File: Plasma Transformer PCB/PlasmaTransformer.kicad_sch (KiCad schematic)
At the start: 86 parts, among them J1 Barrel_Jack_MountingPin, J10 Conn_01x01_Socket, J11 Screw_Terminal_01x01, J12 Screw_Terminal_01x01, J13 Conn_01x01_Socket, J14 Conn_01x01_Socket, J15 Conn_01x01_Socket, J16 Conn_01x01_Socket, J17 Conn_01x01_Socket, J18 Conn_01x01_Socket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

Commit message: WIP rev
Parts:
- removed H2: Hole_Heatsink_Screw, MountingHole:MountingHole_8.4mm_M8, symbol Mechanical:MountingHole
- removed HS1: Heatsink, Library:Heatsink_75x37.5mm_Fischer_SK-594-37.5-AL, symbol Mechanical:Heatsink
- added R11: 0.05, Resistor_SMD:R_2512_6332Metric, symbol Device:R
- added U2: LM358, symbol Amplifier_Operational:LM358
- C10, C7, C8, C9: footprint Capacitor_SMD:C_1812_4532Metric -> Capacitor_SMD:C_1206_3216Metric; MPN CC1812JKNPOCBN221 -> VJ1206A221JBGTW1HV; Manufacturer Yageo -> Vishay
- C11, C12, C21: footprint Capacitor_SMD:C_1812_4532Metric -> Capacitor_SMD:C_0805_2012Metric; MPN VJ1812A102JXFTW1HV -> CL21C102JCFNNNE; Manufacturer Vishay -> Samsung; Voltage 2000V -> 100V
- C3: value 2.7nF -> 3.3nF; footprint Capacitor_SMD:C_1812_4532Metric -> Capacitor_SMD:C_1206_3216Metric; Dielectric X7R -> NP0; MPN 1812GC272KAT1A -> C3216C0G2E332K085AA; Manufacturer Kyocera -> TDK; Voltage 2000V -> 250V
- C4: value 1.8nF -> 3.3nF; footprint Capacitor_SMD:C_1812_4532Metric -> Capacitor_SMD:C_1206_3216Metric; MPN C1812C182JCGACTU -> C3216C0G2E332K085AA; Manufacturer Kemet -> TDK; Voltage 500V -> 250V
- C5, C6: footprint Capacitor_SMD:C_1812_4532Metric -> Capacitor_SMD:C_1206_3216Metric; MPN C1812C182JCGACTU -> CC1206JKNPOZBN182; Manufacturer Kemet -> Yageo; Voltage 500V -> 630V
- Q1: footprint Package_TO_SOT_THT:TO-247-3_Horizontal_TabDown -> Package_TO_SOT_SMD:Infineon_PG-HSOF-8-2_ThermalVias; symbol Transistor_FET_Other:Q_NMOS_Depletion_GDS -> ALibrary:IMT40R025M2HXTMA1; MPN IRFP260NPBF -> IMT40R025M2HXTMA1
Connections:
- net DRAIN: now also Q1.4 (S); no longer Q1.2 (D)
- net GND: now also Q1.2 (SS), Q1.4 (S), R11.2; no longer J1.2
- new net GND-IN: J1.2, R11.1
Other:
- note added: "PLASMA TRANSFORMER REV 6"
- note removed: "Hole for TO-247 screw to heatsink"
- note removed: "PLASMA TRANSFORMER REV 5"
- moved on the sheet: D2, J1, SW1

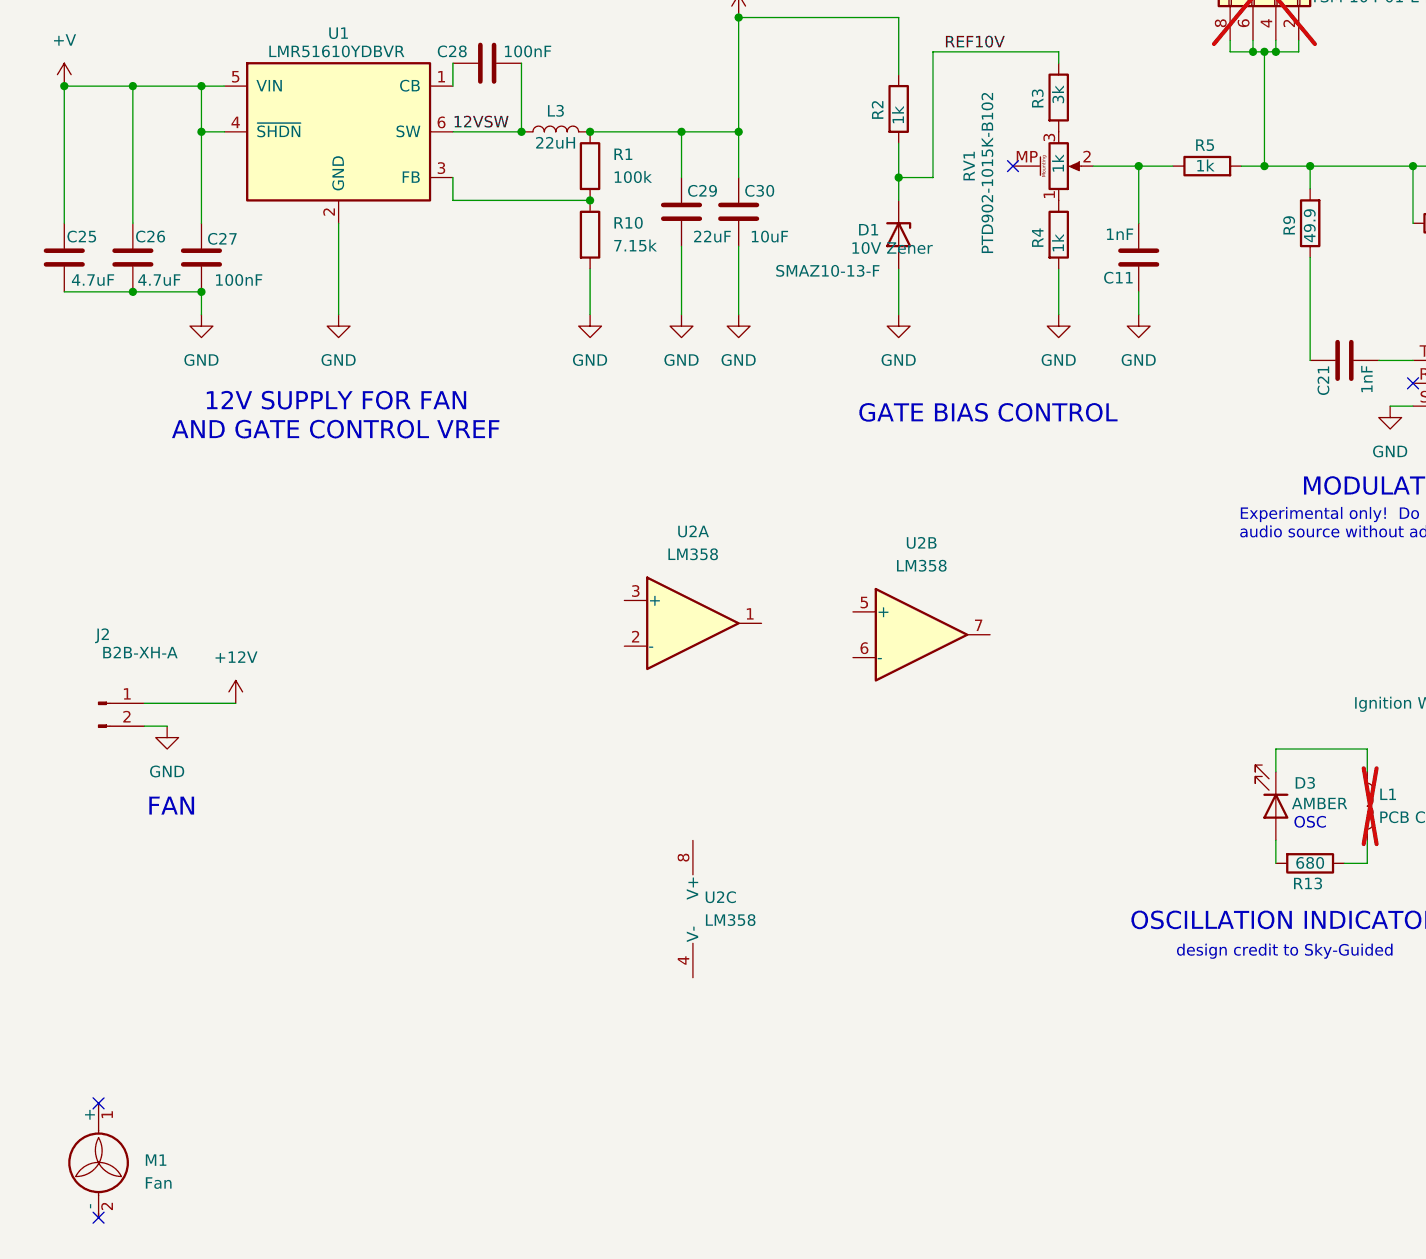
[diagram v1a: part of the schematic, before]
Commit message: mounting holes and silkscreens
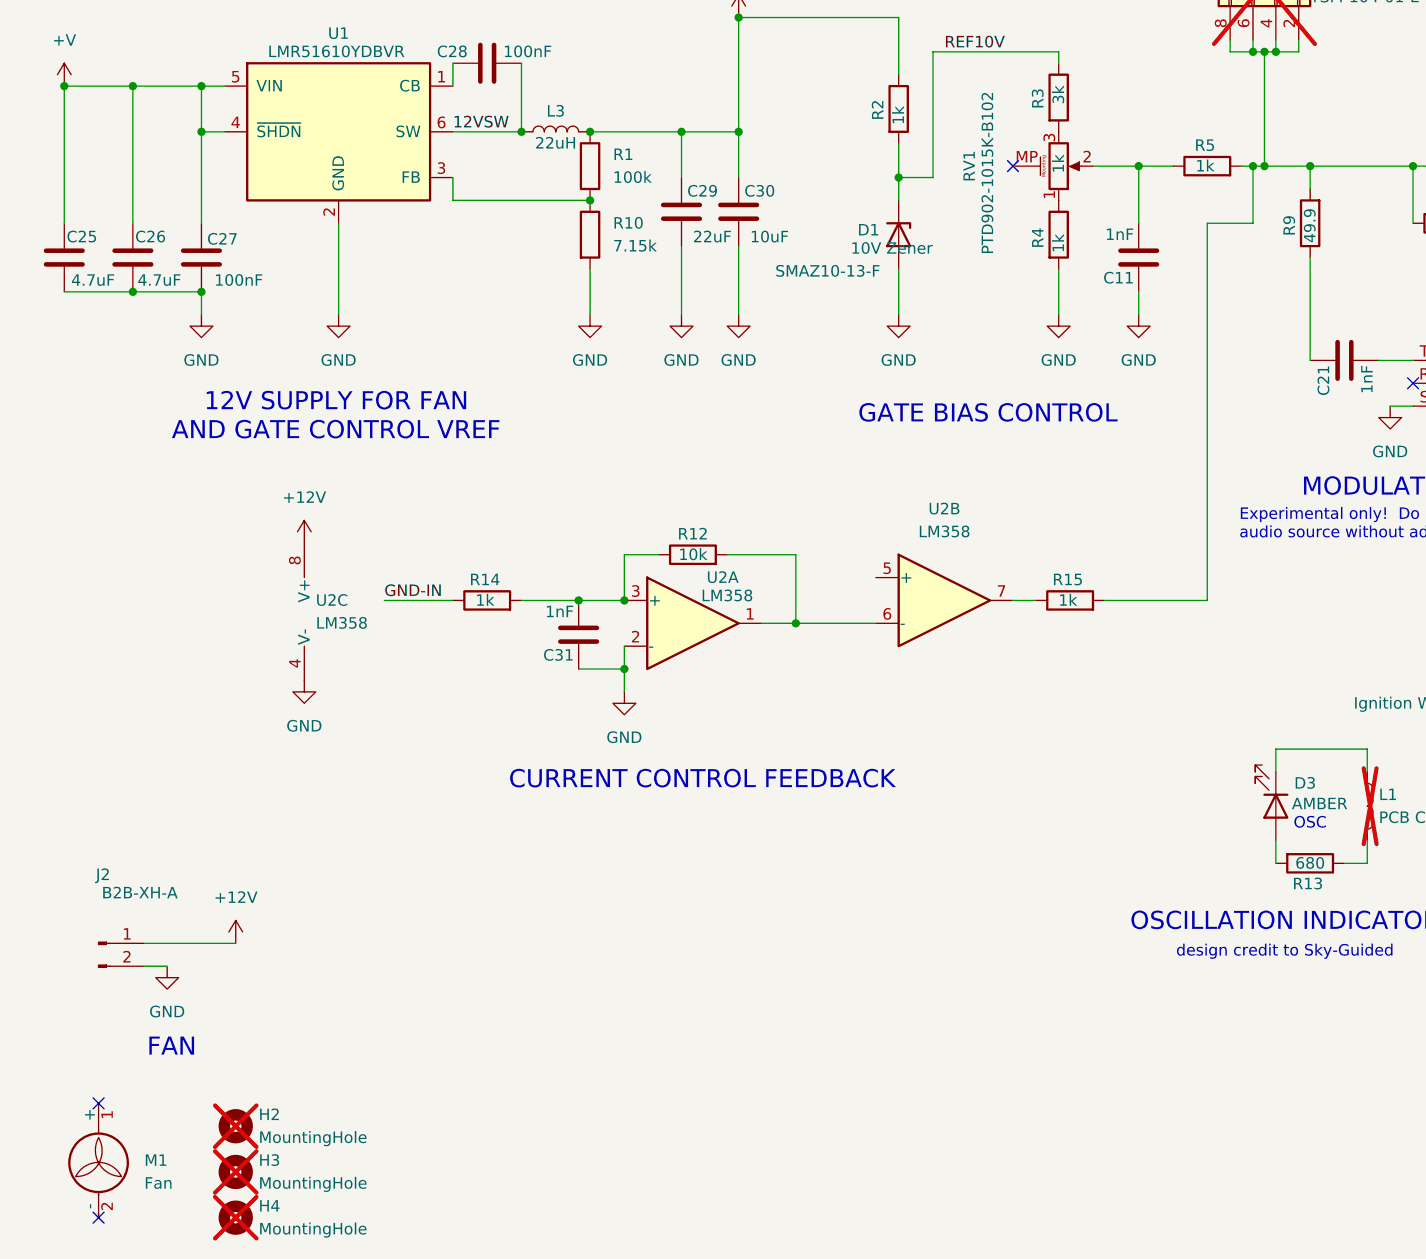
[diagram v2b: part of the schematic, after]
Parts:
- added C31: 1nF, Capacitor_SMD:C_0805_2012Metric, symbol Device:C
- added H2, H3, H4: MountingHole, MountingHole:MountingHole_3.2mm_M3, symbol Mechanical:MountingHole
- added R12: 10k, symbol Device:R
- added R14, R15: 1k, Resistor_SMD:R_0805_2012Metric, symbol Device:R
- Q1: footprint Package_TO_SOT_SMD:Infineon_PG-HSOF-8-2_ThermalVias -> IMT40R025M2HXTMA1
- U2: footprint (none) -> Package_TO_SOT_SMD:SOT-23-8; MPN (none) -> LM358BIDDFR; Manufacturer (none) -> TI
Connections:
- net +12V: now also U2.8 (V+)
- net GATE: now also R15.2
- net GND: now also U2.2 (-), U2.4 (V-), C31.1
- net GND-IN: now also R14.1
- net at U2.6 (-): now also U2.1, R12.2
- net at U2.7: now also R15.1
- net at U2.3 (+): now also C31.2, R12.1, R14.2
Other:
- note added: "CURRENT CONTROL FEEDBACK"
- moved on the sheet: J2, U2B, U2C

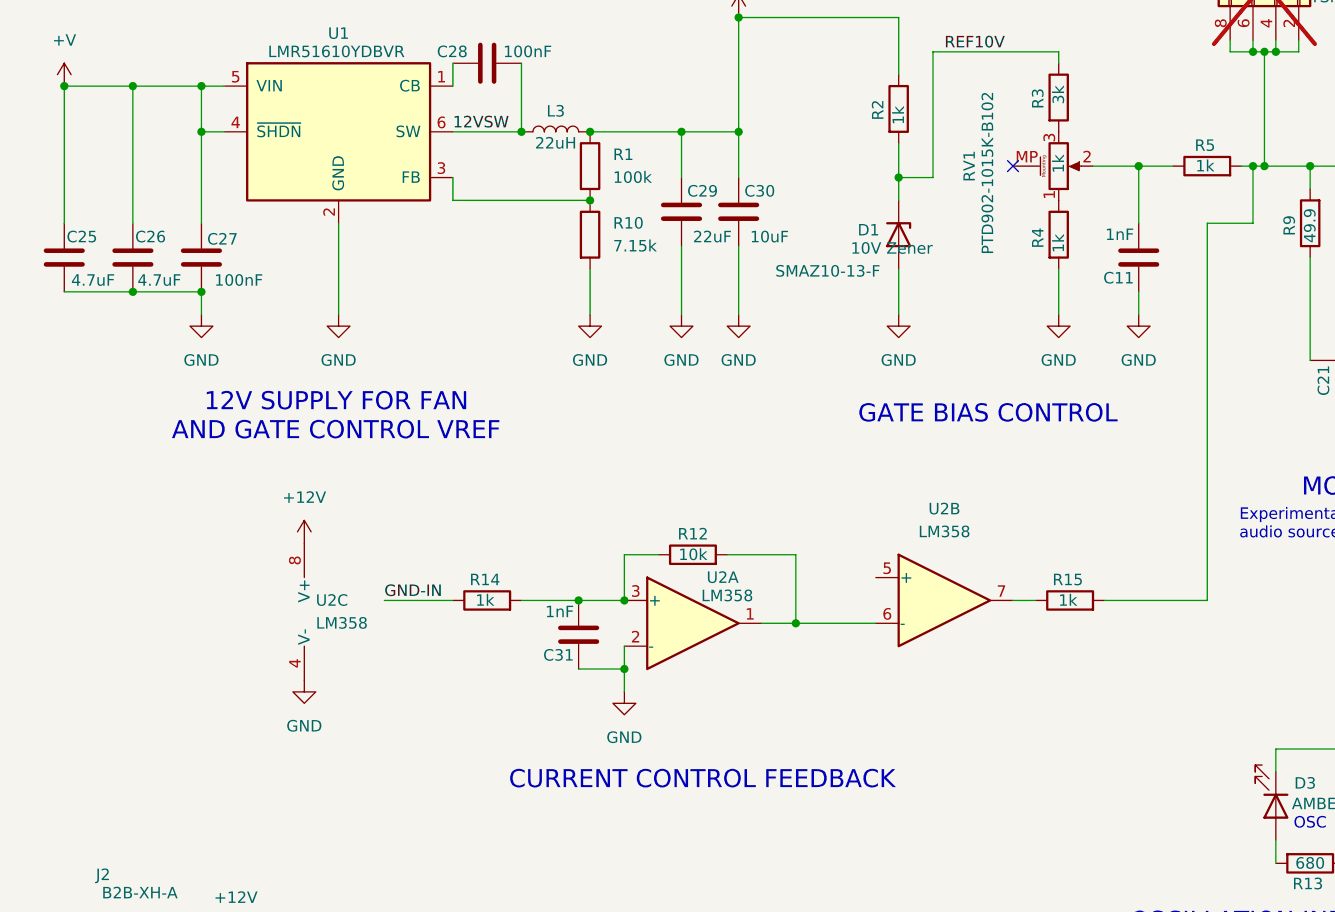
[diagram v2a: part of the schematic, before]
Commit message: layout of feedback circuit
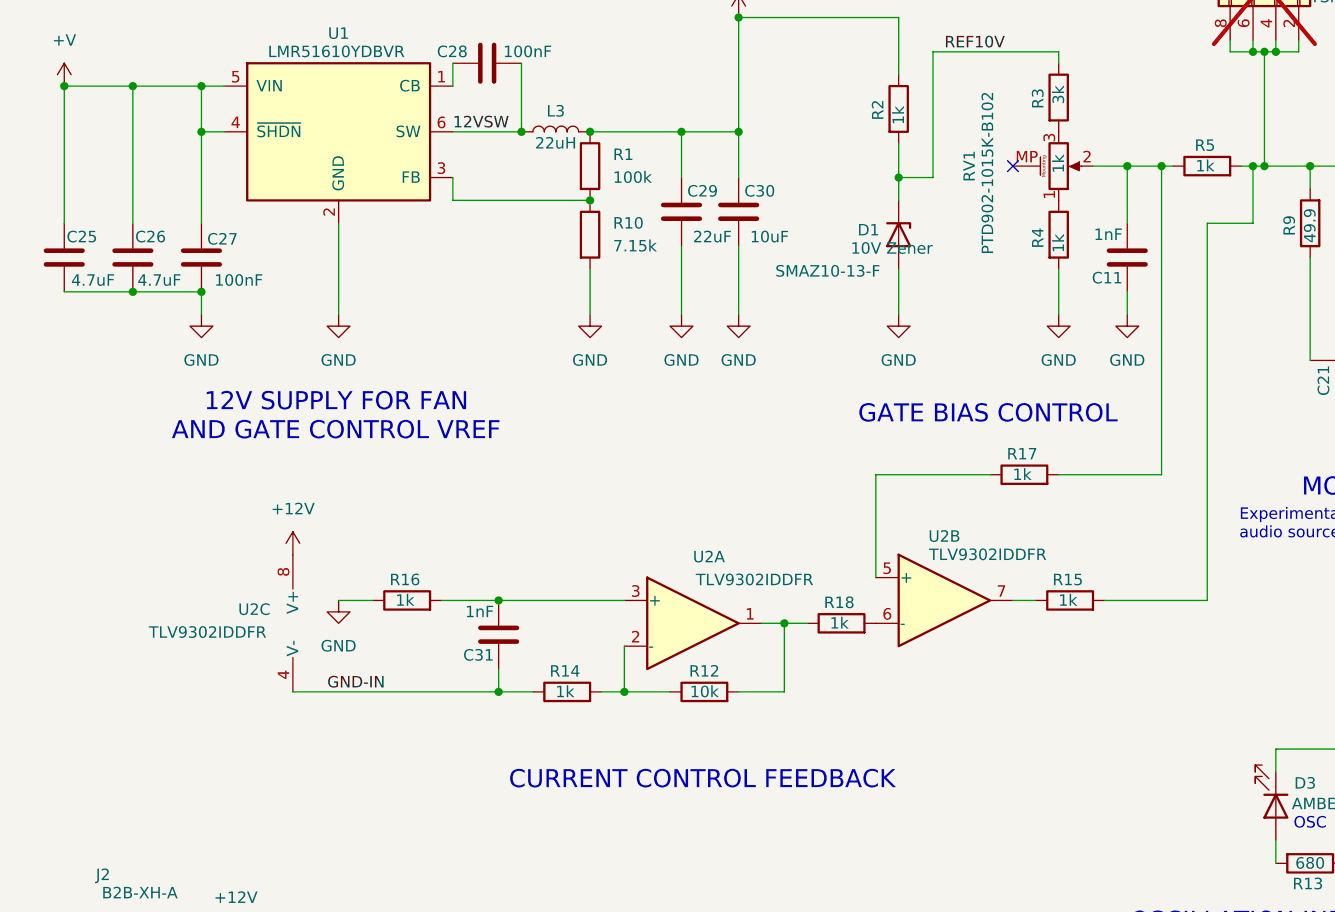
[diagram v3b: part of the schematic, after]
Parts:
- added R16, R17, R18: 1k, Resistor_SMD:R_0805_2012Metric, symbol Device:R
- U2: value LM358 -> TLV9302IDDFR; MPN LM358BIDDFR -> TLV9302IDDFR
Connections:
- net GND: now also R16.1; no longer C31.1, U2.2 (-), U2.4 (V-)
- net GND-IN: now also C31.1, U2.4 (V-)
- net at C11.2, R5.1, RV1.2: now also R17.2
- net at U2.5 (+): now also R17.1
- net at R12.2, U2.1: now also R18.1; no longer U2.6 (-)
- net at R12.1, R14.2: now also U2.2 (-); no longer C31.2, U2.3 (+)
- new net: R18.2, U2.6 (-)
- new net: C31.2, R16.2, U2.3 (+)
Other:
- moved on the sheet: C11, C31, R12, R14, U2C

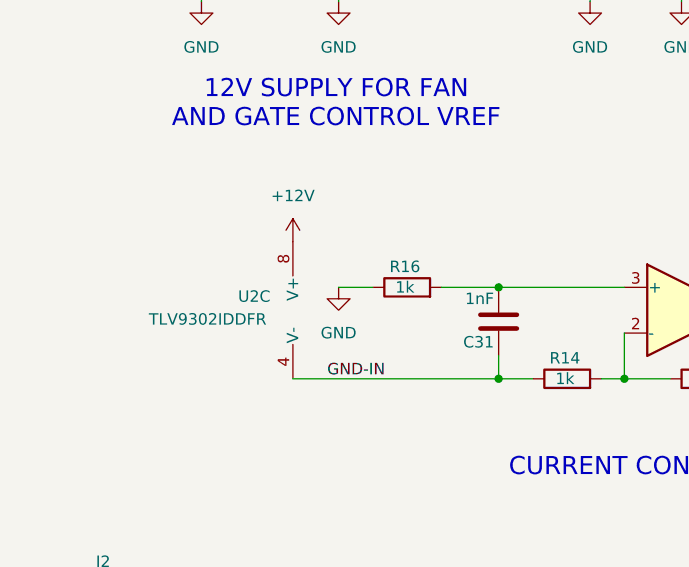
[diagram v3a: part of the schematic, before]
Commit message: routing complete, DRC check OK
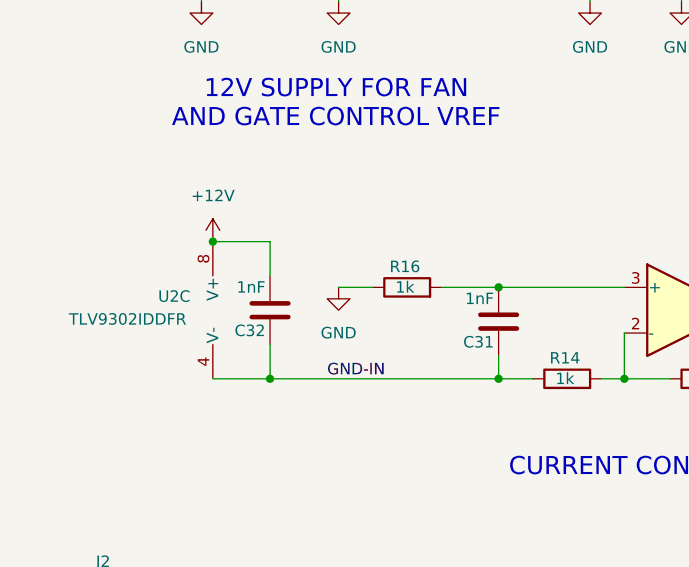
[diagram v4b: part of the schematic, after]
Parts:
- added C32: 1nF, Capacitor_SMD:C_0805_2012Metric, symbol Device:C
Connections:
- net +12V: now also C32.2
- net GND-IN: now also C32.1
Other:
- moved on the sheet: U2C
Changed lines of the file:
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@@
 	)
 	(junction
+		(at 39.37 133.35)
+		(diameter 0)
+		(color 0 0 0 0)
+	)
+	(junction
 		(at 66.04 38.1)
 		(diameter 0)
@@
 	)
 	(junction
+		(at 33.02 118.11)
+		(diameter 0)
+		(color 0 0 0 0)
+	)
+	(junction
 		(at 24.13 88.9)
 		(diameter 0)
@@
 	(wire
 		(pts
-			(xy 41.91 133.35) (xy 64.77 133.35)
-		)
-		(stroke
-			(width 0)
-			(type default)
-		)
-	)
-	(wire
-		(pts
 			(xy 138.43 38.1) (xy 146.05 38.1)
 		)
@@
 	(wire
 		(pts
+			(xy 39.37 129.54) (xy 39.37 133.35)
+		)
+		(stroke
+			(width 0)
+			(type default)
+		)
+	)
+	(wire
+		(pts
 			(xy 104.14 38.1) (xy 111.76 38.1)
 		)
@@
 	(wire
 		(pts
+			(xy 39.37 118.11) (xy 39.37 121.92)
+		)
+		(stroke
+			(width 0)
+			(type default)
+		)
+	)
+	(wire
+		(pts
 			(xy 138.43 48.26) (xy 138.43 45.72)
 		)
@@
 	(wire
 		(pts
+			(xy 39.37 133.35) (xy 64.77 133.35)
+		)
+		(stroke
+			(width 0)
+			(type default)
+		)
+	)
+	(wire
+		(pts
 			(xy 149.86 62.23) (xy 149.86 74.93)
 		)
@@
 	(wire
 		(pts
+			(xy 33.02 133.35) (xy 39.37 133.35)
+		)
+		(stroke
+			(width 0)
+			(type default)
+		)
+	)
+	(wire
+		(pts
 			(xy 76.2 133.35) (xy 78.74 133.35)
 		)
@@
 	(wire
 		(pts
+			(xy 33.02 118.11) (xy 39.37 118.11)
+		)
+		(stroke
+			(width 0)
+			(type default)
+		)
+	)
+	(wire
+		(pts
 			(xy 241.3 142.24) (xy 250.19 142.24)
 		)
@@
 	(symbol
 		(lib_id "power:+1V0")
-		(at 41.91 118.11 0)
+		(at 33.02 118.11 0)
 		(unit 1)
 		(exclude_from_sim no)
@@
 		(dnp no)
 		(property "Reference" "#PWR024"
-			(at 41.91 121.92 0)
+			(at 33.02 121.92 0)
 			(effects
 				(font
@@
 		)
 		(property "Value" "+12V"
-			(at 41.91 113.03 0)
+			(at 33.02 113.03 0)
 			(effects
 				(font
@@
 		)
 		(property "Footprint" ""
-			(at 41.91 118.11 0)
+			(at 33.02 118.11 0)
 			(effects
 				(font
@@
 		)
 		(property "Datasheet" ""
-			(at 41.91 118.11 0)
+			(at 33.02 118.11 0)
 			(effects
 				(font
@@
 		)
 		(property "Description" "Power symbol creates a global label with name \"+1V0\""
-			(at 41.91 118.11 0)
+			(at 33.02 118.11 0)
 			(effects
 				(font
@@
 	)
 	(symbol
+		(lib_id "Device:C")
+		(at 39.37 125.73 180)
+		(unit 1)
+		(exclude_from_sim no)
+		(in_bom yes)
+		(on_board yes)
+		(dnp no)
+		(property "Reference" "C32"
+			(at 38.862 128.016 0)
+			(effects
+				(font
+					(size 1.27 1.27)
+				)
+				(justify left)
+			)
+		)
+		(property "Value" "1nF"
+			(at 38.862 123.19 0)
+			(effects
+				(font
+					(size 1.27 1.27)
+				)
+				(justify left)
+			)
+		)
+		(property "Footprint" "Capacitor_SMD:C_0805_2012Metric"
+			(at 38.4048 121.92 0)
+			(effects
+				(font
+					(size 1.27 1.27)
+				)
+				(hide yes)
+			)
+		)
+		(property "Datasheet" "~"
+			(at 39.37 125.73 0)
+			(effects
+				(font
+					(size 1.27 1.27)
+				)
+				(hide yes)
+			)
+		)
+		(property "Description" "Capacitor 0805"
+			(at 39.37 125.73 0)
+			(effects
+				(font
+					(size 1.27 1.27)
+				)
+				(hide yes)
+			)
+		)
+		(property "Manufacturer" "Samsung"
+			(at 39.37 125.73 0)
+			(effects
+				(font
+					(size 1.27 1.27)
+				)
+				(hide yes)
+			)
+		)
+		(property "MPN" "CL21C102JCFNNNE"
+			(at 38.1 116.84 0)
+			(effects
+				(font
+					(size 1.27 1.27)
+				)
+				(hide yes)
+			)
+		)
+		(property "Dielectric" "C0G"
+			(at 39.37 125.73 0)
+			(effects
+				(font
+					(size 1.27 1.27)
+				)
+				(hide yes)
+			)
+		)
+		(property "Voltage" "100V"
+			(at 39.37 125.73 0)
+			(effects
+				(font
+					(size 1.27 1.27)
+				)
+				(hide yes)
+			)
+		)
+		(pin "1"
+		)
+		(pin "2"
+		)
+		(instances
+			(project "PlasmaTransformer"
+				(path "/3647fd41-d415-410e-af0c-f9576953ab1f"
+					(reference "C32")
+					(unit 1)
+				)
+			)
+		)
+	)
+	(symbol
 		(lib_id "Connector:Conn_01x01_Socket")
 		(at 227.33 69.85 90)
@@
 	(symbol
 		(lib_id "Amplifier_Operational:LM358")
-		(at 44.45 125.73 0)
+		(at 35.56 125.73 0)
 		(unit 3)
 		(exclude_from_sim no)
@@
 		(dnp no)
 		(property "Reference" "U2"
-			(at 35.814 124.206 0)
+			(at 26.924 124.206 0)
 			(effects
 				(font
@@
 		)
 		(property "Value" "TLV9302IDDFR"
-			(at 25.908 126.746 0)
+			(at 17.018 126.746 0)
 			(effects
 				(font
@@
 		)
 		(property "Footprint" "Package_TO_SOT_SMD:SOT-23-8"
-			(at 44.45 125.73 0)
+			(at 35.56 125.73 0)
 			(effects
 				(font
@@
 		)
 		(property "Datasheet" "https://www.ti.com/lit/ds/symlink/tlv9302.pdf"
-			(at 44.45 125.73 0)
+			(at 35.56 125.73 0)
 			(effects
 				(font
@@
 		)
 		(property "Description" "Low-Power, Dual Operational Amplifiers, DIP-8/SOIC-8/TO-99-8"
-			(at 44.45 125.73 0)
+			(at 35.56 125.73 0)
 			(effects
 				(font
@@
 		)
 		(property "MPN" "TLV9302IDDFR"
-			(at 44.45 125.73 0)
+			(at 35.56 125.73 0)
 			(effects
 				(font
@@
 		)
 		(property "Manufacturer" "TI"
-			(at 44.45 125.73 0)
+			(at 35.56 125.73 0)
 			(effects
 				(font
